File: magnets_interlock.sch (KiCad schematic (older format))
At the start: 18 parts

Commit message: Adding DigiKey Library To Project
I think this is adding the DigiKey Library to my local project. I'm not entirely sure however if this will allow you to download it when you clone the repo
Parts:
- removed J? (x3): Conn_Coaxial, symbol Connector:Conn_Coaxial
- removed Q? (x4): 2N7002E, Package_TO_SOT_SMD:SOT-23, symbol Transistor_FET:2N7002E
- removed U?: Magnets_enable, symbol magnets_interlock_library:Magnets_enable
- added +12Supply, -12Supply, Error_Signal_input, Magnets_Enable: BNC_Input_female, conn2_1-1337543-0_TEC, symbol magnets_interlock_library:BNC_Input_female
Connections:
- net labels added: +12VSupply, -12VSupply
- wire segments 9 -> 28
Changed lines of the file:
@@
-$EndComp
-$Comp
-L Transistor_FET:2N7002E Q?
-U 1 1 5EF457D2
-P 1400 1650
-F 0 "Q?" H 1604 1696 50  0000 L CNN
-F 1 "2N7002E" H 1604 1605 50  0000 L CNN
-F 2 "Package_TO_SOT_SMD:SOT-23" H 1600 1575 50  0001 L CIN
-F 3 "http://www.diodes.com/assets/Datasheets/ds30376.pdf" H 1400 1650 50  0001 L CNN
-	1    1400 1650
-	1    0    0    -1
-$EndComp
-$Comp
-L Transistor_FET:2N7002E Q?
-U 1 1 5EF48587
-P 1400 2100
-F 0 "Q?" H 1604 2146 50  0000 L CNN
-F 1 "2N7002E" H 1604 2055 50  0000 L CNN
-F 2 "Package_TO_SOT_SMD:SOT-23" H 1600 2025 50  0001 L CIN
-F 3 "http://www.diodes.com/assets/Datasheets/ds30376.pdf" H 1400 2100 50  0001 L CNN
-	1    1400 2100
-	1    0    0    -1
-$EndComp
-$Comp
-L Transistor_FET:2N7002E Q?
-U 1 1 5EF49704
-P 1400 3350
-F 0 "Q?" H 1604 3396 50  0000 L CNN
-F 1 "2N7002E" H 1604 3305 50  0000 L CNN
-F 2 "Package_TO_SOT_SMD:SOT-23" H 1600 3275 50  0001 L CIN
-F 3 "http://www.diodes.com/assets/Datasheets/ds30376.pdf" H 1400 3350 50  0001 L CNN
-	1    1400 3350
-	1    0    0    -1
-$EndComp
-$Comp
-L Transistor_FET:2N7002E Q?
-U 1 1 5EF4A123
-P 1350 2850
-F 0 "Q?" H 1554 2896 50  0000 L CNN
-F 1 "2N7002E" H 1554 2805 50  0000 L CNN
-F 2 "Package_TO_SOT_SMD:SOT-23" H 1550 2775 50  0001 L CIN
-F 3 "http://www.diodes.com/assets/Datasheets/ds30376.pdf" H 1350 2850 50  0001 L CNN
-	1    1350 2850
-	1    0    0    -1
 $EndComp
 $Comp
@@
 L power:GND #PWR?
 U 1 1 5EF53568
-P 1550 3950
-F 0 "#PWR?" H 1550 3700 50  0001 C CNN
-F 1 "GND" H 1555 3777 50  0000 C CNN
-F 2 "" H 1550 3950 50  0001 C CNN
-F 3 "" H 1550 3950 50  0001 C CNN
-	1    1550 3950
+P 2850 1000
+F 0 "#PWR?" H 2850 750 50  0001 C CNN
+F 1 "GND" H 2855 827 50  0000 C CNN
+F 2 "" H 2850 1000 50  0001 C CNN
+F 3 "" H 2850 1000 50  0001 C CNN
+	1    2850 1000
 	1    0    0    -1
 $EndComp
@@
 Wire Wire Line
 	4750 3050 5250 3050
-$Comp
-L magnets_interlock_library:Magnets_enable U?
-U 1 1 5EF56921
-P 4650 2150
-F 0 "U?" H 4800 2515 50  0000 C CNN
-F 1 "Magnets_enable" H 4800 2424 50  0000 C CNN
-F 2 "" H 4650 2150 50  0001 C CNN
-F 3 "" H 4650 2150 50  0001 C CNN
-	1    4650 2150
-	1    0    0    -1
-$EndComp
-Wire Wire Line
-	4250 2150 3000 2150
-Wire Wire Line
-	3000 2150 3000 3050
 Wire Wire Line
 	3000 3050 3300 3050
 Wire Wire Line
-	5350 2150 6550 2150
-Wire Wire Line
-	6550 2150 6550 2950
-Wire Wire Line
 	6550 2950 6300 2950
-$Comp
-L Connector:Conn_Coaxial J?
-U 1 1 5EF597C8
-P 2500 1400
-F 0 "J?" H 2600 1375 50  0000 L CNN
-F 1 "Conn_Coaxial" H 2600 1284 50  0000 L CNN
-F 2 "" H 2500 1400 50  0001 C CNN
-F 3 " ~" H 2500 1400 50  0001 C CNN
-	1    2500 1400
-	1    0    0    -1
-$EndComp
-$Comp
-L Connector:Conn_Coaxial J?
-U 1 1 5EF59BC3
-P 2500 1950
-F 0 "J?" H 2600 1925 50  0000 L CNN
-F 1 "Conn_Coaxial" H 2600 1834 50  0000 L CNN
-F 2 "" H 2500 1950 50  0001 C CNN
-F 3 " ~" H 2500 1950 50  0001 C CNN
-	1    2500 1950
-	1    0    0    -1
-$EndComp
-$Comp
-L Connector:Conn_Coaxial J?
-U 1 1 5EF5A59A
-P 2500 2500
-F 0 "J?" H 2600 2475 50  0000 L CNN
-F 1 "Conn_Coaxial" H 2600 2384 50  0000 L CNN
-F 2 "" H 2500 2500 50  0001 C CNN
-F 3 " ~" H 2500 2500 50  0001 C CNN
-	1    2500 2500
-	1    0    0    -1
-$EndComp
+Wire Wire Line
+	3000 3050 3000 1650
+Wire Wire Line
+	3000 1650 4450 1650
+Wire Wire Line
+	6550 2950 6550 2150
+Wire Wire Line
+	6550 2150 4200 2150
+Wire Wire Line
+	4200 2150 4200 1750
+Wire Wire Line
+	4200 1750 4450 1750
+$Comp
+L power:GND #PWR?
+U 1 1 5EF4DD5B
+P 4350 2250
+F 0 "#PWR?" H 4350 2000 50  0001 C CNN
+F 1 "GND" H 4355 2077 50  0000 C CNN
+F 2 "" H 4350 2250 50  0001 C CNN
+F 3 "" H 4350 2250 50  0001 C CNN
+	1    4350 2250
+	1    0    0    -1
+$EndComp
+$Comp
+L power:GND #PWR?
+U 1 1 5EF4E6D9
+P 4500 2250
+F 0 "#PWR?" H 4500 2000 50  0001 C CNN
+F 1 "GND" H 4505 2077 50  0000 C CNN
+F 2 "" H 4500 2250 50  0001 C CNN
+F 3 "" H 4500 2250 50  0001 C CNN
+	1    4500 2250
+	1    0    0    -1
+$EndComp
+Wire Wire Line
+	4350 2250 4350 1850
+Wire Wire Line
+	4350 1850 4450 1850
+Wire Wire Line
+	4450 1950 4450 2250
+Wire Wire Line
+	4450 2250 4500 2250
+$Comp
+L magnets_interlock_library:BNC_Input_female Magnets_Enable
+U 1 1 5EF69399
+P 4450 1650
+F 0 "Magnets_Enable" H 4978 1553 60  0000 L CNN
+F 1 "BNC_Input_female" H 4978 1447 60  0000 L CNN
+F 2 "conn2_1-1337543-0_TEC" H 4850 1590 60  0001 C CNN
+F 3 "" H 4450 1650 60  0000 C CNN
+	1    4450 1650
+	1    0    0    -1
+$EndComp
+$Comp
+L magnets_interlock_library:BNC_Input_female +12Supply
+U 1 1 5EF69FE4
+P 1050 3200
+F 0 "+12Supply" H 1578 3103 60  0000 L CNN
+F 1 "BNC_Input_female" H 1578 2997 60  0000 L CNN
+F 2 "conn2_1-1337543-0_TEC" H 1450 3140 60  0001 C CNN
+F 3 "" H 1050 3200 60  0000 C CNN
+	1    1050 3200
+	1    0    0    -1
+$EndComp
+$Comp
+L magnets_interlock_library:BNC_Input_female -12Supply
+U 1 1 5EF6A95F
+P 1050 4100
+F 0 "-12Supply" H 1578 4003 60  0000 L CNN
+F 1 "BNC_Input_female" H 1578 3897 60  0000 L CNN
+F 2 "conn2_1-1337543-0_TEC" H 1450 4040 60  0001 C CNN
+F 3 "" H 1050 4100 60  0000 C CNN
+	1    1050 4100
+	1    0    0    -1
+$EndComp
+$Comp
+L power:GND #PWR?
+U 1 1 5EF6B6AB
+P 750 3350
+F 0 "#PWR?" H 750 3100 50  0001 C CNN
+F 1 "GND" H 755 3177 50  0000 C CNN
+F 2 "" H 750 3350 50  0001 C CNN
+F 3 "" H 750 3350 50  0001 C CNN
+	1    750  3350
+	1    0    0    -1
+$EndComp
+Wire Wire Line
+	1050 3300 1050 3350
+Connection ~ 1050 3400
+Wire Wire Line
+	1050 3400 1050 3500
+Wire Wire Line
+	750  3350 1050 3350
+Wire Wire Line
+	1050 3350 1050 3400
+Connection ~ 1050 3350
+$Comp
+L power:GND #PWR?
+U 1 1 5EF6EDE4
+P 700 4350
+F 0 "#PWR?" H 700 4100 50  0001 C CNN
+F 1 "GND" H 705 4177 50  0000 C CNN
+F 2 "" H 700 4350 50  0001 C CNN
+F 3 "" H 700 4350 50  0001 C CNN
+	1    700  4350
+	1    0    0    -1
+$EndComp
+Wire Wire Line
+	1050 4200 1050 4300
+Connection ~ 1050 4300
+Wire Wire Line
+	1050 4300 1050 4350
+Wire Wire Line
+	700  4350 1050 4350
+Connection ~ 1050 4350
+Wire Wire Line
+	1050 4350 1050 4400
+$Comp
+L magnets_interlock_library:BNC_Input_female Error_Signal_input
+U 1 1 5EF7182C
+P 1000 5050
+F 0 "Error_Signal_input" H 1528 4953 60  0000 L CNN
+F 1 "BNC_Input_female" H 1528 4847 60  0000 L CNN
+F 2 "conn2_1-1337543-0_TEC" H 1400 4990 60  0001 C CNN
+F 3 "" H 1000 5050 60  0000 C CNN
+	1    1000 5050
+	1    0    0    -1
+$EndComp
+Wire Wire Line
+	1000 5150 1000 5250
+Connection ~ 1000 5250
+Wire Wire Line
+	1000 5250 1000 5350
+$Comp
+L power:GND #PWR?
+U 1 1 5EF72CF4
+P 700 5250
+F 0 "#PWR?" H 700 5000 50  0001 C CNN
+F 1 "GND" H 705 5077 50  0000 C CNN
+F 2 "" H 700 5250 50  0001 C CNN
+F 3 "" H 700 5250 50  0001 C CNN
+	1    700  5250
+	1    0    0    -1
+$EndComp
+Wire Wire Line
+	700  5250 1000 5250
+Text GLabel 1050 2900 1    50   Input ~ 0
++12VSupply
+Wire Wire Line
+	1050 2900 1050 3200
+Text GLabel 1050 3850 0    50   Input ~ 0
+-12VSupply
+Wire Wire Line
+	1050 3850 1050 4100
 $EndSCHEMATC

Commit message: Adding Isolation to Power and Signal Inputs
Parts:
- removed -12Supply: BNC_Input_female, conn2_1-1337543-0_TEC, symbol magnets_interlock_library:BNC_Input_female
- added PS?: ROE-2405S, CONV_ROE-2405S, symbol ROE-2405S:ROE-2405S
- added U?: PEM2-S24-S24-S, CONV_PEM2-S24-S24-S, symbol PEM2-S24-S24-S:PEM2-S24-S24-S
- added U?: Si8610BC-B-IS, SOIC-8_SIL, symbol 2020-06-25_21-51-44:Si8610BC-B-IS
- renumbered +12Supply to +24Supply
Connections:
- net labels added: +24V
- net labels removed: +12VSupply, -12VSupply
- wire segments 28 -> 40
- no-connect marks 0 -> 2
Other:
- moved on the sheet: +24Supply, Error_Signal_input, Magnets_Enable, U?A

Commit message: Buffered Ouptut of Isolator. Created sub-sheet for relays
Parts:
- removed D? (x2): LED, symbol Device:LED
- removed Magnets_Enable: BNC_Input_female, conn2_1-1337543-0_TEC, symbol magnets_interlock_library:BNC_Input_female
- removed R? (x2): R, symbol Device:R
- removed SW? (x2): SW_Push, symbol Switch:SW_Push
- removed U? (x2): Safety_Relay_DPDT, symbol magnets_interlock_library:Safety_Relay_DPDT
- removed U?: 74AUC2G08, symbol 74xGxx:74AUC2G08
- removed U?: 74AHC1G08, symbol 74xGxx:74AHC1G08
- added C? (x4): 0.1u, symbol Device:C
- added C?: 0.33u, symbol Device:C
- added C?: 10u, symbol Device:C
- added C? (x2): 1u, symbol Device:C
- added U?: LM2904DR, D8, symbol 2020-06-25_23-20-23:LM2904DR
- added U?: UA78M05CDCYR, DCY4_TEX, symbol 2020-06-25_22-55-44:UA78M05CDCYR
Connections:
- net labels added: ErrorSignal
- wire segments 40 -> 71

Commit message: New Power and Signal Isolation
Making 5V standard and using Enrique parts
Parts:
- added U?: Si8640BD-B-IS, SOIC-16W_SIL, symbol 2020-06-26_17-59-50:Si8640BD-B-IS
- added U?: SR4D4005, RELAY10-5MM-6.5MM, symbol 2020-06-26_17-54-09:SR4D4005
- added VT?: NXE1S0505MC-R7, VREG_NXE1S0505MC-R7, symbol NXE1S0505MC-R7:NXE1S0505MC-R7
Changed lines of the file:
@@
 $EndDescr
-$Comp
-L power:GND #PWR?
-U 1 1 5EF53568
-P 6100 1050
-F 0 "#PWR?" H 6100 800 50  0001 C CNN
-F 1 "GND" H 6105 877 50  0000 C CNN
-F 2 "" H 6100 1050 50  0001 C CNN
-F 3 "" H 6100 1050 50  0001 C CNN
-	1    6100 1050
-	1    0    0    -1
-$EndComp
 $Comp
 L magnets_interlock_library:BNC_Input_female +24Supply
@@
 Connection ~ 4400 2600
 $Sheet
-S 5600 3750 2650 1250
+S 8550 4950 2650 1250
 U 5EF588A2
 F0 "Relays and Mag Enable" 50
@@
 Wire Wire Line
 	3250 2350 3250 3150
+$Comp
+L NXE1S0505MC-R7:NXE1S0505MC-R7 VT?
+U 1 1 5EF669F4
+P 1900 6400
+F 0 "VT?" H 1900 6767 50  0000 C CNN
+F 1 "NXE1S0505MC-R7" H 1900 6676 50  0000 C CNN
+F 2 "VREG_NXE1S0505MC-R7" H 1900 6400 50  0001 L BNN
+F 3 "muRata" H 1900 6400 50  0001 L BNN
+	1    1900 6400
+	1    0    0    -1
+$EndComp
+$Comp
+L 2020-06-26_17-54-09:SR4D4005 U?
+U 1 1 5EF68D6D
+P 4750 1150
+F 0 "U?" H 5650 1638 60  0000 C CNN
+F 1 "SR4D4005" H 5650 1532 60  0000 C CNN
+F 2 "RELAY10-5MM-6.5MM" H 5650 1490 60  0001 C CNN
+F 3 "" H 4750 1150 60  0000 C CNN
+	1    4750 1150
+	1    0    0    -1
+$EndComp
+$Comp
+L 2020-06-26_17-59-50:Si8640BD-B-IS U?
+U 1 1 5EF654E5
+P 8000 1350
+F 0 "U?" H 9200 1737 60  0000 C CNN
+F 1 "Si8640BD-B-IS" H 9200 1631 60  0000 C CNN
+F 2 "SOIC-16W_SIL" H 9200 1590 60  0001 C CNN
+F 3 "" H 8000 1350 60  0000 C CNN
+	1    8000 1350
+	1    0    0    -1
+$EndComp
 $EndSCHEMATC

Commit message: Adding 5V components
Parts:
- removed VT?: NXE1S0505MC-R7, VREG_NXE1S0505MC-R7, symbol NXE1S0505MC-R7:NXE1S0505MC-R7
- added J?: 691508110303, 691508110303, symbol 691508110303:691508110303
- added VT?: NXJ1S0505MC-R7, VREG_NXJ1S0505MC-R7, symbol NXJ1S0505MC-R7:NXJ1S0505MC-R7
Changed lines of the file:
@@
 	3250 2350 3250 3150
-$Comp
-L NXE1S0505MC-R7:NXE1S0505MC-R7 VT?
-U 1 1 5EF669F4
-P 1900 6400
-F 0 "VT?" H 1900 6767 50  0000 C CNN
-F 1 "NXE1S0505MC-R7" H 1900 6676 50  0000 C CNN
-F 2 "VREG_NXE1S0505MC-R7" H 1900 6400 50  0001 L BNN
-F 3 "muRata" H 1900 6400 50  0001 L BNN
-	1    1900 6400
-	1    0    0    -1
-$EndComp
 $Comp
 L 2020-06-26_17-54-09:SR4D4005 U?
@@
 	1    0    0    -1
 $EndComp
+$Comp
+L NXJ1S0505MC-R7:NXJ1S0505MC-R7 VT?
+U 1 1 5EF6FDB4
+P 1500 6100
+F 0 "VT?" H 1500 5825 50  0000 C CNN
+F 1 "NXJ1S0505MC-R7" H 1500 5734 50  0000 C CNN
+F 2 "VREG_NXJ1S0505MC-R7" H 1050 5700 50  0001 L BNN
+F 3 "muRata" H 1500 6100 50  0001 L BNN
+	1    1500 6100
+	1    0    0    -1
+$EndComp
+$Comp
+L 691508110303:691508110303 J?
+U 1 1 5EF7A439
+P 1600 7000
+F 0 "J?" H 1780 7046 50  0000 L CNN
+F 1 "691508110303" H 1780 6955 50  0000 L CNN
+F 2 "691508110303" H 1600 7000 50  0001 L BNN
+F 3 "" H 1600 7000 50  0001 C CNN
+	1    1600 7000
+	1    0    0    -1
+$EndComp

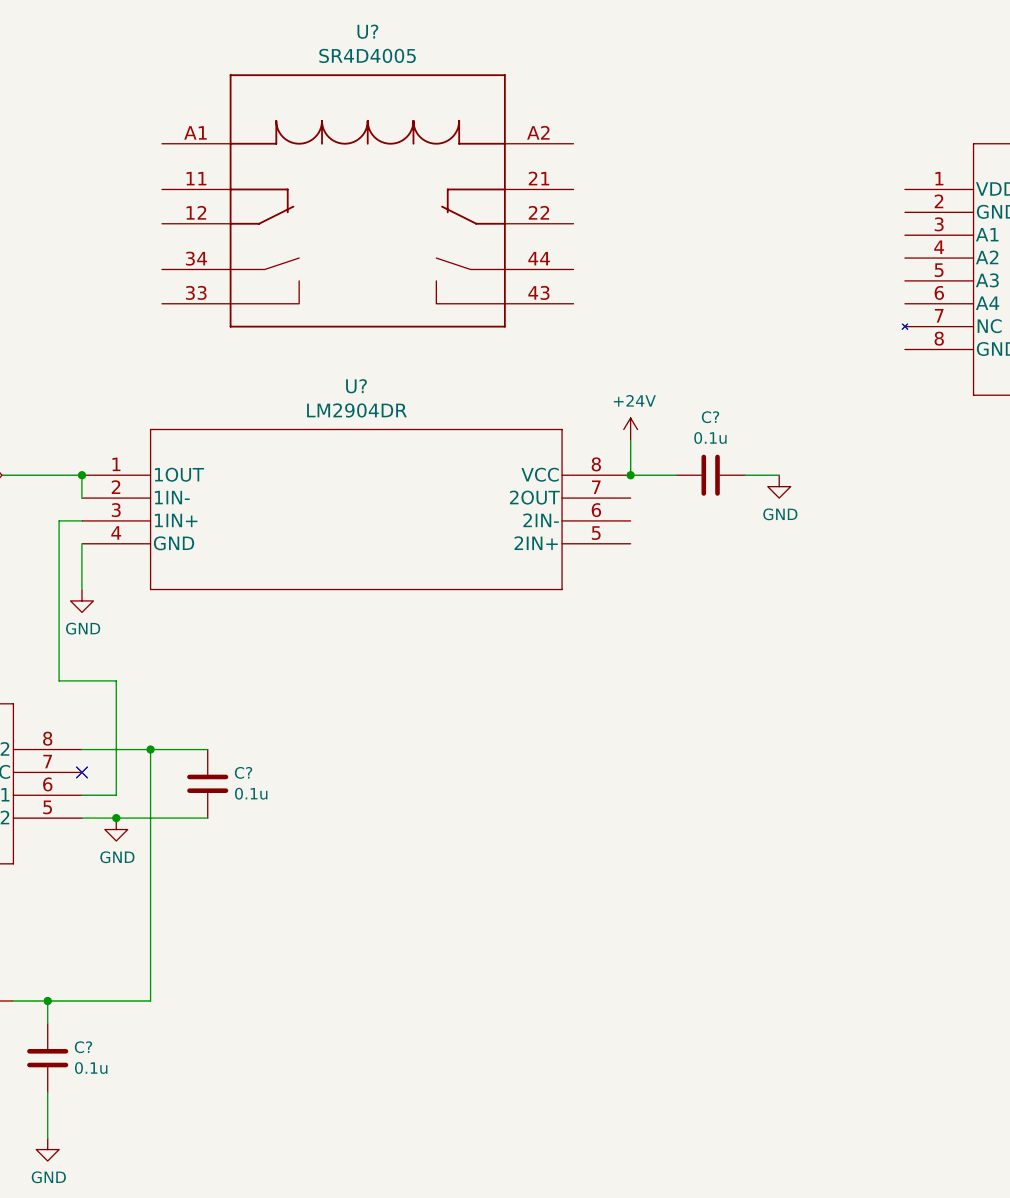
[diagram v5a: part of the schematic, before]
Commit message: Saving a few things
Before I get rid of the +24 Volt stuff
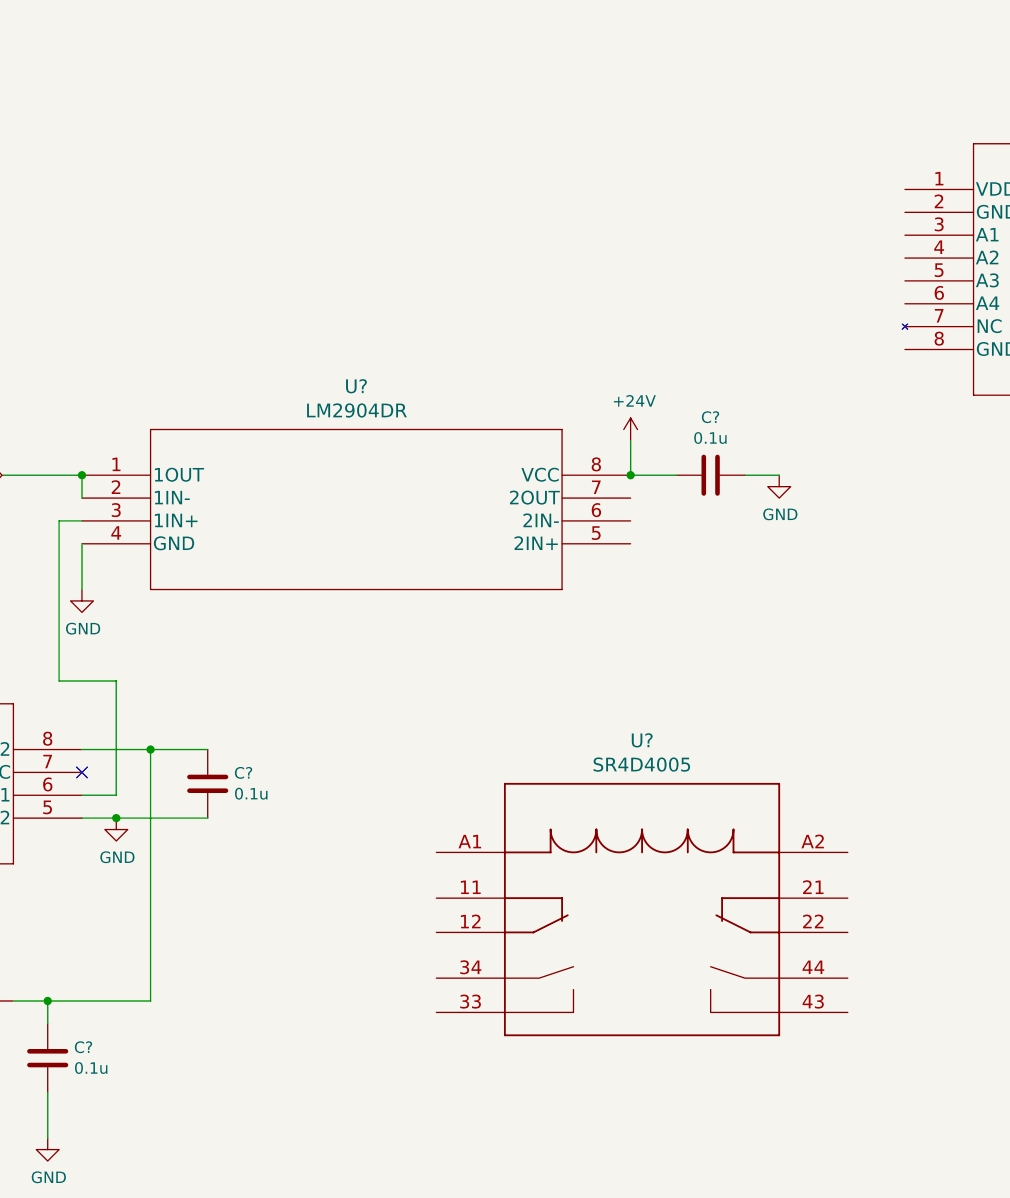
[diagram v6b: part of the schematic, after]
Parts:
- removed U?: SR4D4005, RELAY10-5MM-6.5MM, symbol 2020-06-26_17-54-09:SR4D4005
- added U?: SR4D4005, RELAY10-5MM-6.5MM, symbol 2020-06-26_17-54-09:SR4D4005
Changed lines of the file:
@@
 	3250 2350 3250 3150
-$Comp
-L 2020-06-26_17-54-09:SR4D4005 U?
-U 1 1 5EF68D6D
-P 4750 1150
-F 0 "U?" H 5650 1638 60  0000 C CNN
-F 1 "SR4D4005" H 5650 1532 60  0000 C CNN
-F 2 "RELAY10-5MM-6.5MM" H 5650 1490 60  0001 C CNN
-F 3 "" H 4750 1150 60  0000 C CNN
-	1    4750 1150
-	1    0    0    -1
-$EndComp
 $Comp
 L 2020-06-26_17-59-50:Si8640BD-B-IS U?
@@
 	1    0    0    -1
 $EndComp
+$Comp
+L 2020-06-26_17-54-09:SR4D4005 U?
+U 1 1 5EF80687
+P 5950 4250
+F 0 "U?" H 6850 4738 60  0000 C CNN
+F 1 "SR4D4005" H 6850 4632 60  0000 C CNN
+F 2 "RELAY10-5MM-6.5MM" H 6850 4590 60  0001 C CNN
+F 3 "" H 5950 4250 60  0000 C CNN
+	1    5950 4250
+	1    0    0    -1
+$EndComp

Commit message: Rough Draft of Relay Circuit
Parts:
- removed +24Supply, Error_Signal_input: BNC_Input_female, conn2_1-1337543-0_TEC, symbol magnets_interlock_library:BNC_Input_female
- removed C? (x4): 0.1u, symbol Device:C
- removed C?: 0.33u, symbol Device:C
- removed C?: 10u, symbol Device:C
- removed C? (x2): 1u, symbol Device:C
- removed PS?: ROE-2405S, CONV_ROE-2405S, symbol ROE-2405S:ROE-2405S
- removed U?: LM2904DR, D8, symbol 2020-06-25_23-20-23:LM2904DR
- removed U?: PEM2-S24-S24-S, CONV_PEM2-S24-S24-S, symbol PEM2-S24-S24-S:PEM2-S24-S24-S
- removed U?: SR4D4005, RELAY10-5MM-6.5MM, symbol 2020-06-26_17-54-09:SR4D4005
- removed U?: Si8610BC-B-IS, SOIC-8_SIL, symbol 2020-06-25_21-51-44:Si8610BC-B-IS
- removed U?: UA78M05CDCYR, DCY4_TEX, symbol 2020-06-25_22-55-44:UA78M05CDCYR
- removed VT?: NXJ1S0505MC-R7, VREG_NXJ1S0505MC-R7, symbol NXJ1S0505MC-R7:NXJ1S0505MC-R7
- added ERR_In, J?: BNC_Input_female, conn2_1-1337543-0_TEC, symbol magnets_interlock_library:BNC_Input_female
- added R?: R, symbol Device:R
- added S?: CL-SB-12B-01T, CL-SB-12B, symbol CL-SB-12B-01T:CL-SB-12B-01T
- added VT? (x3): NXJ1S0505MC-R7, VREG_NXJ1S0505MC-R7, symbol NXJ1S0505MC-R7:NXJ1S0505MC-R7
- gave numbers to parts that had none: 1
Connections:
- net GND: now also U?.11 (B4), U?.12 (B3), U?.15 (GND2), U?.9 (GND2), R?.1, S?.3, VT?.7 (-VOUT), VT?.7 (-VOUT)
- net at U?.1 (VDD1): now also VT?.8 (+VOUT)
- net at U?.10 (EN2): now also R?.2, S?.2
- net +5VOut1: now reaches U?.16 (VDD2)
- net +5VOut1: now also S?.1, VT?.8 (+VOUT)
- net at U?.2 (GND1): now also U?.5 (A3), U?.6 (A4), U?.8 (GND1), ERR_In.2 (BNC_Shield), ERR_In.3 (shield), ERR_In.4 (shield), VT?.7 (-VOUT)
- net at U?.3 (A1): now also U?.4 (A2), ERR_In.1 (Center_Pin)
- net +5VIN: now reaches PWR_In.1
- net +5VIN: now also VT?.3 (+VIN), VT?.3 (+VIN), VT?.3 (+VIN)
- net PWR_GND_IN: now reaches PWR_In.3
- net PWR_GND_IN: now also VT?.1 (-VIN), VT?.1 (-VIN), VT?.1 (-VIN)
- new net +5VOut2: VT?.8 (+VOUT)
- no-connect marks 2 -> 1
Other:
- moved on the sheet: PWR_In, U?
